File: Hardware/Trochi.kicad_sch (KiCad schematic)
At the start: 54 parts, among them IC1 ICM-42688-P, J1 JST-SH, J2 JST-SH, J3 JST PH, J4 JST-SH, J5 JST-SH, J6 JST_SH, Q1 AO3401A, Q2 AO3400A, Q3 AO3400A, Q4 AO3400A, Q5 AO3400A, Q6 AO3400A, SW1 SW_SPDT, U1 ME6211C33M5, U3 YX-SMD5020

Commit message: chore: assign footprints to all connectors
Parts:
- C1, C10, C11, C3, C5, C6, C7, C8, C9: footprint (none) -> Capacitor_SMD:C_0402_1005Metric
- C2: footprint (none) -> Capacitor_SMD:C_1206_3216Metric
- C4: footprint (none) -> Capacitor_SMD:C_0805_2012Metric
- D1, D2, D3, D4, D6: footprint (none) -> Diode_SMD:D_SMA
- D5: footprint (none) -> LED_SMD:LED_0603_1608Metric
- J1, J2, J4, J5: footprint (none) -> trochi_footprint:CONN-SMD_2P-P1.00_SM02B-SRSS-TB-LF-SN
- J3: footprint (none) -> trochi_footprint:CONN-SMD_P2.00_S2B-PH-SM4-TB-LF-SN
- J6: footprint (none) -> trochi_footprint:CONN-SMD_4P-P1.00_SM04B-SRSS-TB-LF-SN
- R1, R10, R11, R12, R13, R14, R15, R16, R17, R18, R19, R2, R3, R4, R5, R6, R7, R8, R9: footprint (none) -> Resistor_SMD:R_0402_1005Metric
- SW1: footprint (none) -> trochi_footprint:SW-TH_K3-1293S-E2
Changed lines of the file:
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@@
 			)
 		)
-		(property "Footprint" ""
+		(property "Footprint" "Resistor_SMD:R_0402_1005Metric"
 			(at 45.72 180.34 0)
 			(hide yes)
@@
 			)
 		)
-		(property "Footprint" ""
+		(property "Footprint" "Resistor_SMD:R_0402_1005Metric"
 			(at 104.14 149.86 0)
 			(hide yes)
@@
 			)
 		)
-		(property "Footprint" ""
+		(property "Footprint" "Resistor_SMD:R_0402_1005Metric"
 			(at 195.58 53.34 0)
 			(hide yes)
@@
 			)
 		)
-		(property "Footprint" ""
+		(property "Footprint" "Capacitor_SMD:C_0402_1005Metric"
 			(at 139.7 40.64 0)
 			(hide yes)
@@
 			)
 		)
-		(property "Footprint" ""
+		(property "Footprint" "Capacitor_SMD:C_0805_2012Metric"
 			(at 129.54 40.64 0)
 			(hide yes)
@@
 			)
 		)
-		(property "Footprint" ""
+		(property "Footprint" "Capacitor_SMD:C_0402_1005Metric"
 			(at 167.64 163.83 0)
 			(hide yes)
@@
 			)
 		)
-		(property "Footprint" ""
+		(property "Footprint" "Resistor_SMD:R_0402_1005Metric"
 			(at 116.84 149.86 0)
 			(hide yes)
@@
 			)
 		)
-		(property "Footprint" ""
+		(property "Footprint" "Resistor_SMD:R_0402_1005Metric"
 			(at 33.02 24.13 0)
 			(hide yes)
@@
 			)
 		)
-		(property "Footprint" ""
+		(property "Footprint" "Diode_SMD:D_SMA"
 			(at 264.16 35.56 90)
 			(hide yes)
@@
 			)
 		)
-		(property "Footprint" ""
+		(property "Footprint" "Resistor_SMD:R_0402_1005Metric"
 			(at 81.28 58.42 0)
 			(hide yes)
@@
 			)
 		)
-		(property "Footprint" ""
+		(property "Footprint" "trochi_footprint:CONN-SMD_2P-P1.00_SM02B-SRSS-TB-LF-SN"
 			(at 262.89 20.32 0)
 			(hide yes)
@@
 			)
 		)
-		(property "Footprint" ""
+		(property "Footprint" "Capacitor_SMD:C_0402_1005Metric"
 			(at 257.81 135.89 0)
 			(hide yes)
@@
 			)
 		)
-		(property "Footprint" ""
+		(property "Footprint" "Resistor_SMD:R_0402_1005Metric"
 			(at 43.18 24.13 0)
 			(hide yes)
@@
 			)
 		)
-		(property "Footprint" ""
+		(property "Footprint" "Capacitor_SMD:C_0402_1005Metric"
 			(at 71.12 40.64 0)
 			(hide yes)
@@
 			)
 		)
-		(property "Footprint" ""
+		(property "Footprint" "Diode_SMD:D_SMA"
 			(at 205.74 35.56 90)
 			(hide yes)
@@
 			)
 		)
-		(property "Footprint" ""
+		(property "Footprint" "trochi_footprint:SW-TH_K3-1293S-E2"
 			(at 54.61 24.13 0)
 			(hide yes)
@@
 			)
 		)
-		(property "Footprint" ""
+		(property "Footprint" "Capacitor_SMD:C_0402_1005Metric"
 			(at 46.99 40.64 0)
 			(hide yes)
@@
 			)
 		)
-		(property "Footprint" ""
+		(property "Footprint" "Diode_SMD:D_SMA"
 			(at 264.16 83.82 90)
 			(hide yes)
@@
 			)
 		)
-		(property "Footprint" ""
+		(property "Footprint" "Diode_SMD:D_SMA"
 			(at 53.34 163.83 90)
 			(hide yes)
@@
 			)
 		)
-		(property "Footprint" ""
+		(property "Footprint" "Capacitor_SMD:C_1206_3216Metric"
 			(at 58.42 40.64 0)
 			(hide yes)
@@
 			)
 		)
-		(property "Footprint" ""
+		(property "Footprint" "Capacitor_SMD:C_0402_1005Metric"
 			(at 95.25 58.42 0)
 			(hide yes)
@@
 			)
 		)
-		(property "Footprint" ""
+		(property "Footprint" "Diode_SMD:D_SMA"
 			(at 205.74 83.82 90)
 			(hide yes)
@@
 			)
 		)
-		(property "Footprint" ""
+		(property "Footprint" "Resistor_SMD:R_0402_1005Metric"
 			(at 182.88 93.98 0)
 			(hide yes)
@@
 			)
 		)
-		(property "Footprint" ""
+		(property "Footprint" "Resistor_SMD:R_0402_1005Metric"
 			(at 81.28 40.64 0)
 			(hide yes)
@@
 			)
 		)
-		(property "Footprint" ""
+		(property "Footprint" "Resistor_SMD:R_0402_1005Metric"
 			(at 182.88 45.72 0)
 			(hide yes)
@@
 			)
 		)
-		(property "Footprint" ""
+		(property "Footprint" "Resistor_SMD:R_0402_1005Metric"
 			(at 254 101.6 0)
 			(hide yes)
@@
 			)
 		)
-		(property "Footprint" ""
+		(property "Footprint" "Resistor_SMD:R_0402_1005Metric"
 			(at 241.3 93.98 0)
 			(hide yes)
@@
 			)
 		)
-		(property "Footprint" ""
+		(property "Footprint" "LED_SMD:LED_0603_1608Metric"
 			(at 33.02 120.65 90)
 			(hide yes)
@@
 			)
 		)
-		(property "Footprint" ""
+		(property "Footprint" "Resistor_SMD:R_0402_1005Metric"
 			(at 212.09 129.54 0)
 			(hide yes)
@@
 			)
 		)
-		(property "Footprint" ""
+		(property "Footprint" "Resistor_SMD:R_0402_1005Metric"
 			(at 195.58 101.6 0)
 			(hide yes)
@@
 			)
 		)
-		(property "Footprint" ""
+		(property "Footprint" "Resistor_SMD:R_0402_1005Metric"
 			(at 110.49 149.86 0)
 			(hide yes)
@@
 			)
 		)
-		(property "Footprint" ""
+		(property "Footprint" "Resistor_SMD:R_0402_1005Metric"
 			(at 254 53.34 0)
 			(hide yes)
@@
 			)
 		)
-		(property "Footprint" ""
+		(property "Footprint" "Capacitor_SMD:C_0402_1005Metric"
 			(at 257.81 148.59 0)
 			(hide yes)
@@
 			)
 		)
-		(property "Footprint" ""
+		(property "Footprint" "trochi_footprint:CONN-SMD_2P-P1.00_SM02B-SRSS-TB-LF-SN"
 			(at 262.89 68.58 0)
 			(hide yes)
@@
 			)
 		)
-		(property "Footprint" ""
+		(property "Footprint" "Capacitor_SMD:C_0402_1005Metric"
 			(at 151.13 40.64 0)
 			(hide yes)
@@
 			)
 		)
-		(property "Footprint" ""
+		(property "Footprint" "trochi_footprint:CONN-SMD_2P-P1.00_SM02B-SRSS-TB-LF-SN"
 			(at 204.47 20.32 0)
 			(hide yes)
@@
 			)
 		)
-		(property "Footprint" ""
+		(property "Footprint" "Resistor_SMD:R_0402_1005Metric"
 			(at 33.02 128.27 0)
 			(hide yes)
@@
 			)
 		)
-		(property "Footprint" ""
+		(property "Footprint" "Resistor_SMD:R_0402_1005Metric"
 			(at 39.37 173.99 0)
 			(hide yes)
@@
 			)
 		)
-		(property "Footprint" ""
+		(property "Footprint" "Resistor_SMD:R_0402_1005Metric"
 			(at 241.3 45.72 0)
 			(hide yes)
@@
 			)
 		)
-		(property "Footprint" ""
+		(property "Footprint" "Capacitor_SMD:C_0402_1005Metric"
 			(at 158.75 163.83 0)
 			(hide yes)
@@
 			)
 		)
-		(property "Footprint" ""
+		(property "Footprint" "trochi_footprint:CONN-SMD_P2.00_S2B-PH-SM4-TB-LF-SN"
 			(at 17.78 38.1 0)
 			(hide yes)
@@
 			)
 		)
-		(property "Footprint" ""
+		(property "Footprint" "trochi_footprint:CONN-SMD_2P-P1.00_SM02B-SRSS-TB-LF-SN"
 			(at 204.47 68.58 0)
 			(hide yes)
@@
 			)
 		)
-		(property "Footprint" ""
+		(property "Footprint" "trochi_footprint:CONN-SMD_4P-P1.00_SM04B-SRSS-TB-LF-SN"
 			(at 39.37 88.9 0)
 			(hide yes)

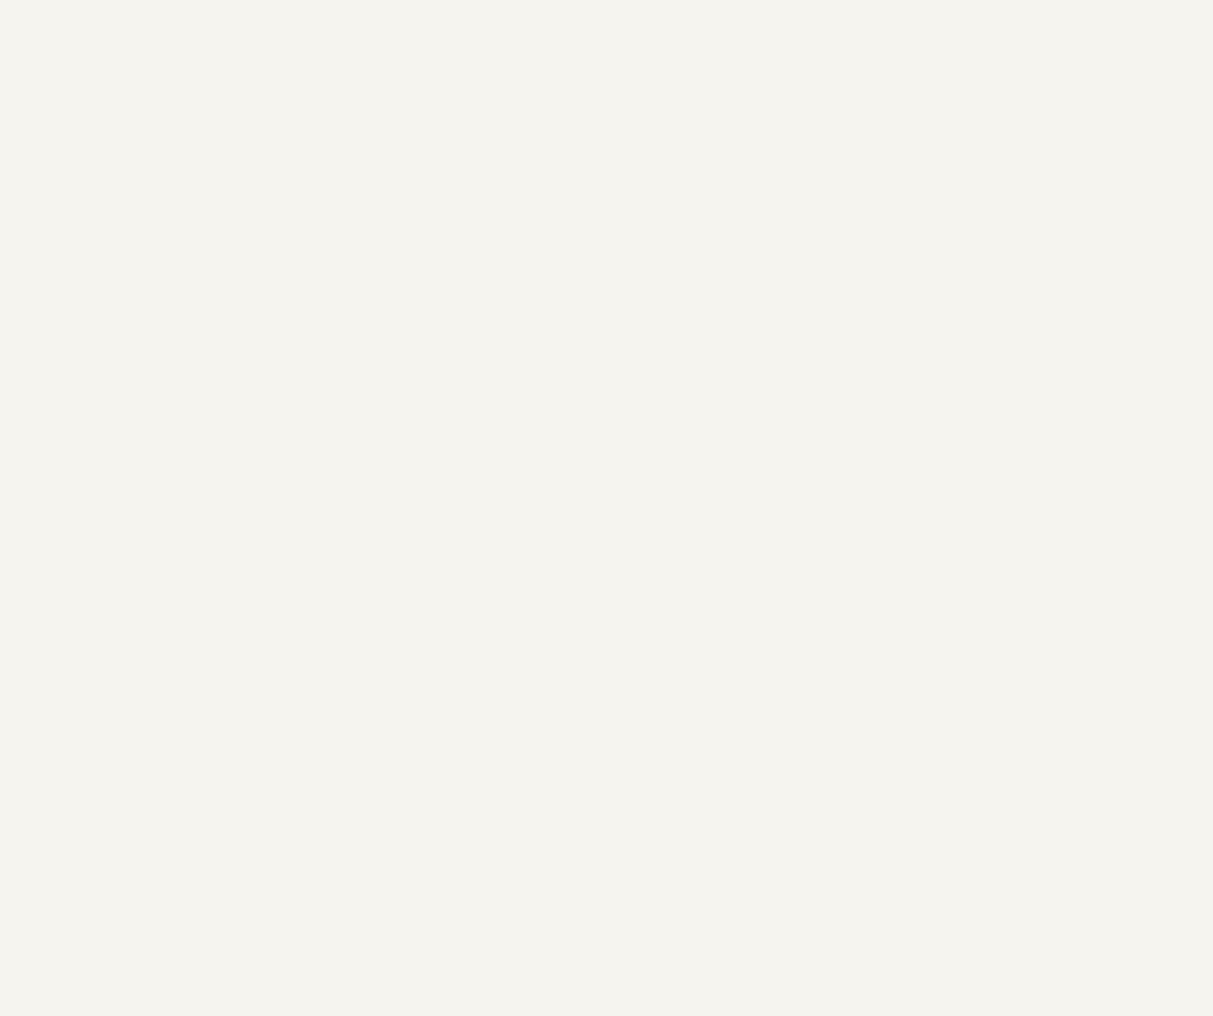
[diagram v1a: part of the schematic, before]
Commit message: feat: update symbol and footprint for TF-021B-H265 in library
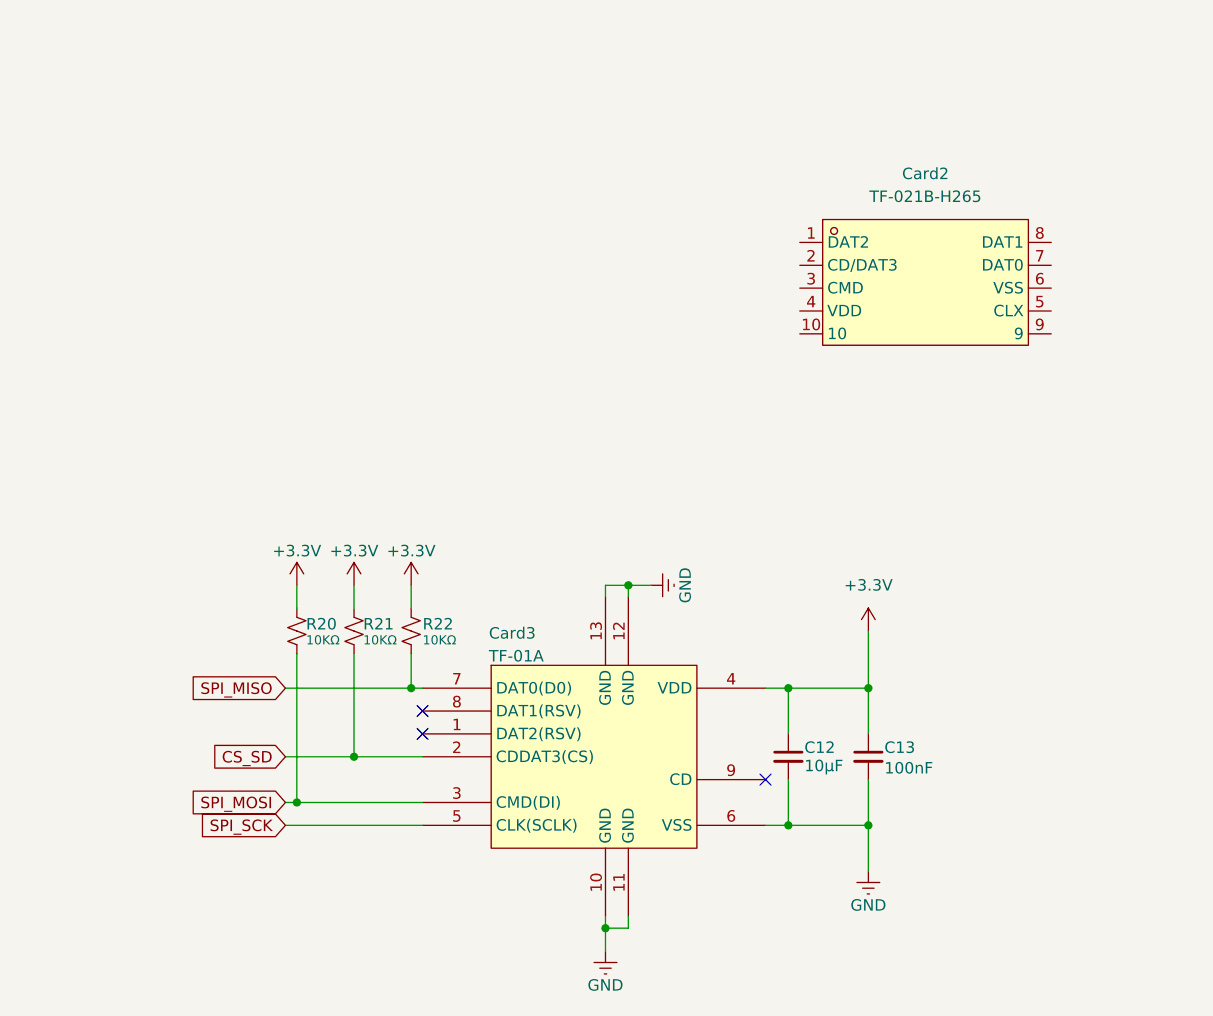
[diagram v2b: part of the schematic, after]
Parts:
- added C12: 10µF, Capacitor_SMD:C_0402_1005Metric, symbol Device:C_Small
- added C13: 100nF, Capacitor_SMD:C_0402_1005Metric, symbol Device:C_Small
- added Card2: TF-021B-H265, trochi_footprint:TF-SMD_TF-021B-H265, symbol trochi_sym:TF-021B-H265
- added Card3: TF-01A, trochi_footprint:TF-SMD_TF-01A, symbol trochi_sym:TF-01A
- added R20, R21, R22: 10KΩ, Resistor_SMD:R_0402_1005Metric, symbol Device:R_Small_US
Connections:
- net +3.3V: now also C12.1, C13.1, Card3.4 (VDD), R20.1, R21.1, R22.1
- net CS_SD: now also Card3.2 (CDDAT3(CS)), R21.2
- net GND: now also C12.2, C13.2, Card3.10 (GND), Card3.11 (GND), Card3.12 (GND), Card3.13 (GND), Card3.6 (VSS)
- net SPI_MISO: now also Card3.7 (DAT0(D0)), R22.2
- net SPI_MOSI: now also Card3.3 (CMD(DI)), R20.2
- net SPI_SCK: now also Card3.5 (CLK(SCLK))
- no-connect marks 7 -> 10

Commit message: feat: add TF-021B-H265 microSD card to schematic
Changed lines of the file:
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@@
+	)
+	(symbol
+		(lib_id "trochi_sym:TF-021B-H265")
+		(at 106.68 255.27 0)
+		(unit 1)
+		(body_style 1)
+		(exclude_from_sim no)
+		(in_bom yes)
+		(on_board yes)
+		(in_pos_files yes)
+		(dnp no)
+		(fields_autoplaced yes)
+		(property "Reference" "Card2"
+			(at 102.87 243.84 0)
+			(show_name no)
+			(do_not_autoplace no)
+			(effects
+				(font
+					(size 1.27 1.27)
+				)
+			)
+		)
+		(property "Value" "TF-021B-H265"
+			(at 102.87 246.38 0)
+			(show_name no)
+			(do_not_autoplace no)
+			(effects
+				(font
+					(size 1.27 1.27)
+				)
+			)
+		)
+		(property "Footprint" "trochi_footprint:TF-SMD_TF-021B-H265"
+			(at 106.68 269.24 0)
+			(hide yes)
+			(show_name no)
+			(do_not_autoplace no)
+			(effects
+				(font
+					(size 1.27 1.27)
+				)
+			)
+		)
+		(property "Datasheet" "https://lcsc.com/product-detail/New-Arrivals_SOFNG-TF-021B-H265_C498185.html"
+			(at 106.68 271.78 0)
+			(hide yes)
+			(show_name no)
+			(do_not_autoplace no)
+			(effects
+				(font
+					(size 1.27 1.27)
+				)
+			)
+		)
+		(property "Description" ""
+			(at 106.68 255.27 0)
+			(hide yes)
+			(show_name no)
+			(do_not_autoplace no)
+			(effects
+				(font
+					(size 1.27 1.27)
+				)
+			)
+		)
+		(property "Manufacturer" "SOFNG(硕方)"
+			(at 106.68 274.32 0)
+			(hide yes)
+			(show_name no)
+			(do_not_autoplace no)
+			(effects
+				(font
+					(size 1.27 1.27)
+				)
+			)
+		)
+		(property "MPN" "TF-021B-H265"
+			(at 106.68 276.86 0)
+			(hide yes)
+			(show_name no)
+			(do_not_autoplace no)
+			(effects
+				(font
+					(size 1.27 1.27)
+				)
+			)
+		)
+		(property "LCSC Part" "C498185"
+			(at 106.68 279.4 0)
+			(hide yes)
+			(show_name no)
+			(do_not_autoplace no)
+			(effects
+				(font
+					(size 1.27 1.27)
+				)
+			)
+		)
+		(pin "1"
+		)
+		(pin "5"
+		)
+		(pin "7"
+		)
+		(pin "3"
+		)
+		(pin "4"
+		)
+		(pin "8"
+		)
+		(pin "6"
+		)
+		(pin "2"
+		)
+		(instances
+			(project "Trochi"
+				(path "/a5119cab-c33d-484e-b542-18705d0dc8d0"
+					(reference "Card2")
+					(unit 1)
+				)
+			)
+		)
 	)
 	(symbol
@@
 					(unit 1)
 				)
-			)
-		)
-	)
-	(symbol
-		(lib_id "trochi_sym:TF-021B-H265")
-		(at 137.16 240.03 0)
-		(unit 1)
-		(body_style 1)
-		(exclude_from_sim no)
-		(in_bom yes)
-		(on_board yes)
-		(in_pos_files yes)
-		(dnp no)
-		(fields_autoplaced yes)
-		(property "Reference" "Card2"
-			(at 137.16 228.6 0)
-			(show_name no)
-			(do_not_autoplace no)
-			(effects
-				(font
-					(size 1.27 1.27)
-				)
-			)
-		)
-		(property "Value" "TF-021B-H265"
-			(at 137.16 231.14 0)
-			(show_name no)
-			(do_not_autoplace no)
-			(effects
-				(font
-					(size 1.27 1.27)
-				)
-			)
-		)
-		(property "Footprint" "trochi_footprint:TF-SMD_TF-021B-H265"
-			(at 137.16 254 0)
-			(hide yes)
-			(show_name no)
-			(do_not_autoplace no)
-			(effects
-				(font
-					(size 1.27 1.27)
-				)
-			)
-		)
-		(property "Datasheet" "https://lcsc.com/product-detail/New-Arrivals_SOFNG-TF-021B-H265_C498185.html"
-			(at 137.16 256.54 0)
-			(hide yes)
-			(show_name no)
-			(do_not_autoplace no)
-			(effects
-				(font
-					(size 1.27 1.27)
-				)
-			)
-		)
-		(property "Description" ""
-			(at 137.16 240.03 0)
-			(hide yes)
-			(show_name no)
-			(do_not_autoplace no)
-			(effects
-				(font
-					(size 1.27 1.27)
-				)
-			)
-		)
-		(property "Manufacturer" "SOFNG(硕方)"
-			(at 137.16 259.08 0)
-			(hide yes)
-			(show_name no)
-			(do_not_autoplace no)
-			(effects
-				(font
-					(size 1.27 1.27)
-				)
-			)
-		)
-		(property "MPN" "TF-021B-H265"
-			(at 137.16 261.62 0)
-			(hide yes)
-			(show_name no)
-			(do_not_autoplace no)
-			(effects
-				(font
-					(size 1.27 1.27)
-				)
-			)
-		)
-		(property "LCSC Part" "C498185"
-			(at 137.16 264.16 0)
-			(hide yes)
-			(show_name no)
-			(do_not_autoplace no)
-			(effects
-				(font
-					(size 1.27 1.27)
-				)
-			)
-		)
-		(pin "6"
-		)
-		(pin "8"
-		)
-		(pin "5"
-		)
-		(pin "7"
-		)
-		(pin "1"
-		)
-		(pin "2"
-		)
-		(pin "9"
-		)
-		(pin "4"
-		)
-		(pin "10"
-		)
-		(pin "3"
-		)
-		(instances
-			(project "Trochi"
-				(path "/a5119cab-c33d-484e-b542-18705d0dc8d0"
-					(reference "Card2")
-					(unit 1)
-				)
